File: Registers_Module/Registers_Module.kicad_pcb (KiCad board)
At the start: 2 copper layers, 95.9 x 90.2 mm, 45 parts, among them U1 74LS245, U12 74LS245, U13 74LS173, U14 74LS173, U2 74LS173, U3 74LS173

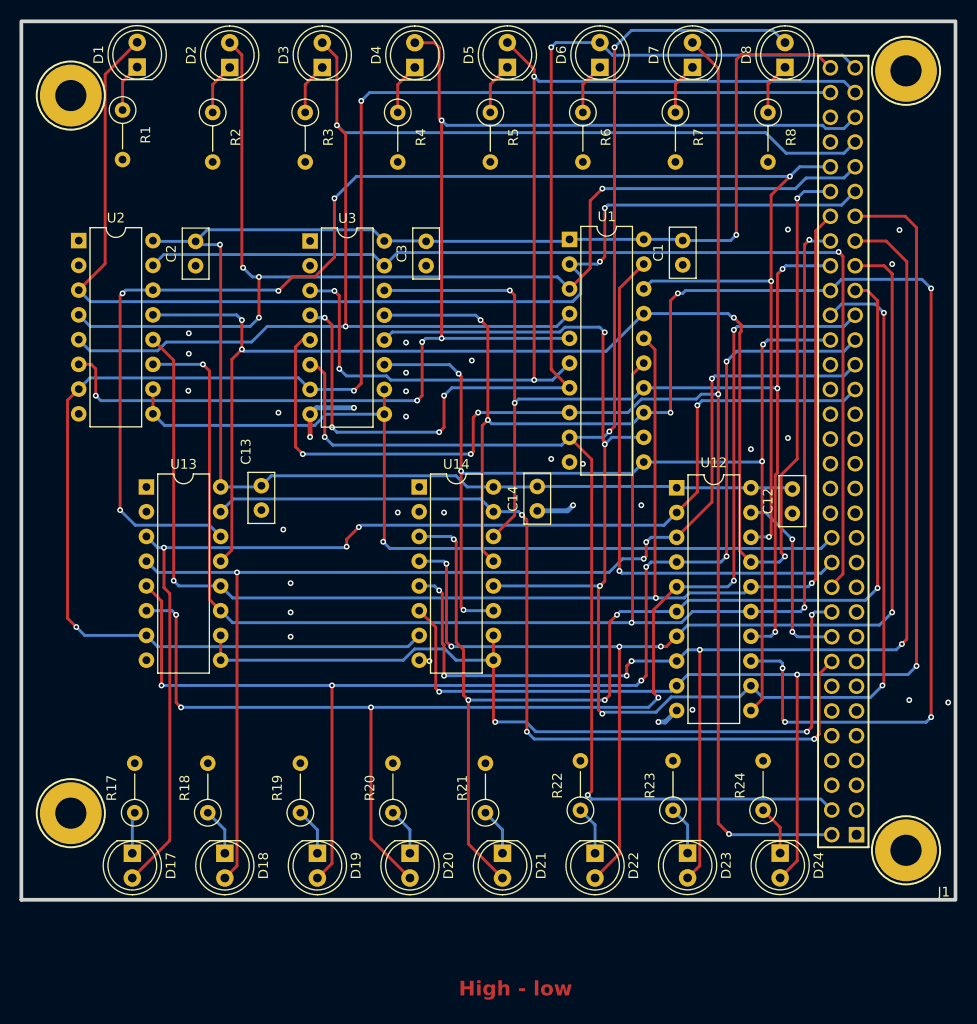
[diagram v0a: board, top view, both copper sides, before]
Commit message: merge and updates the Register module
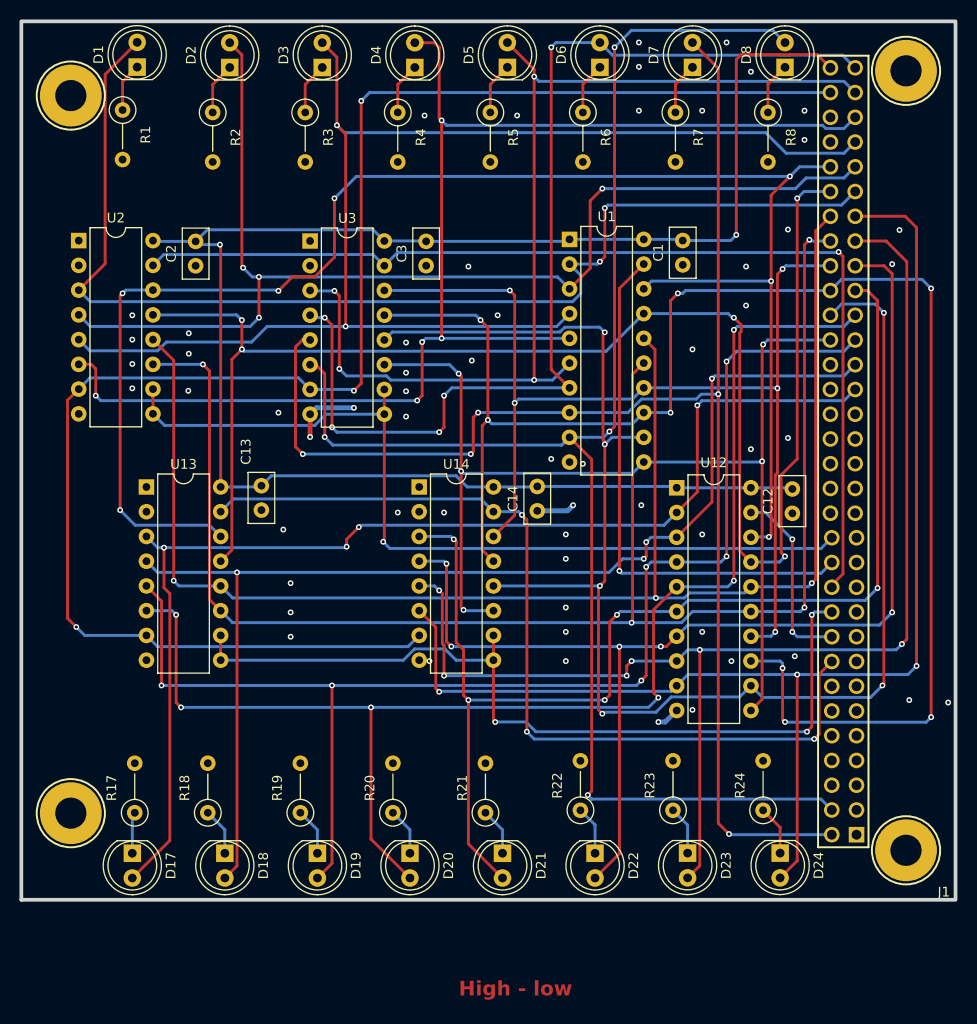
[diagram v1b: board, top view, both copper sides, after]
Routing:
- net GND: vias 31 -> 59
